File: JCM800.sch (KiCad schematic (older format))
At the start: 102 parts, among them U1 ECC83, U2 ECC83, U3 ECC83, U4 EL84, U5 EL84

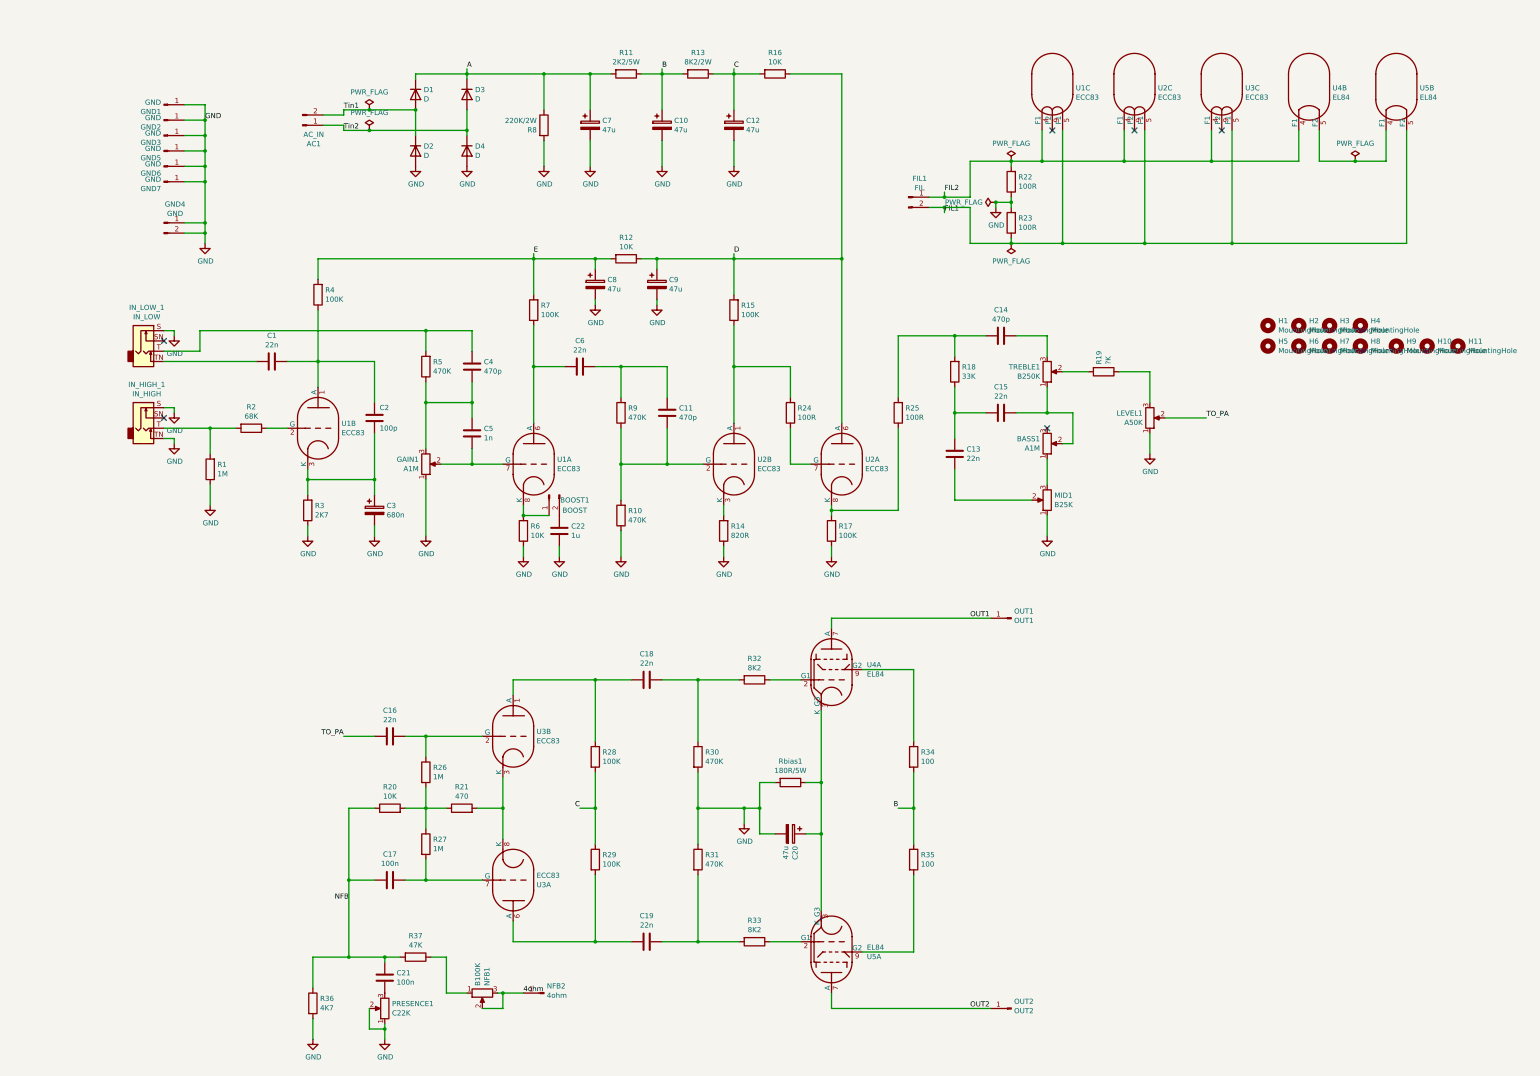
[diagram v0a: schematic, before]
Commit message: New grounding scheme
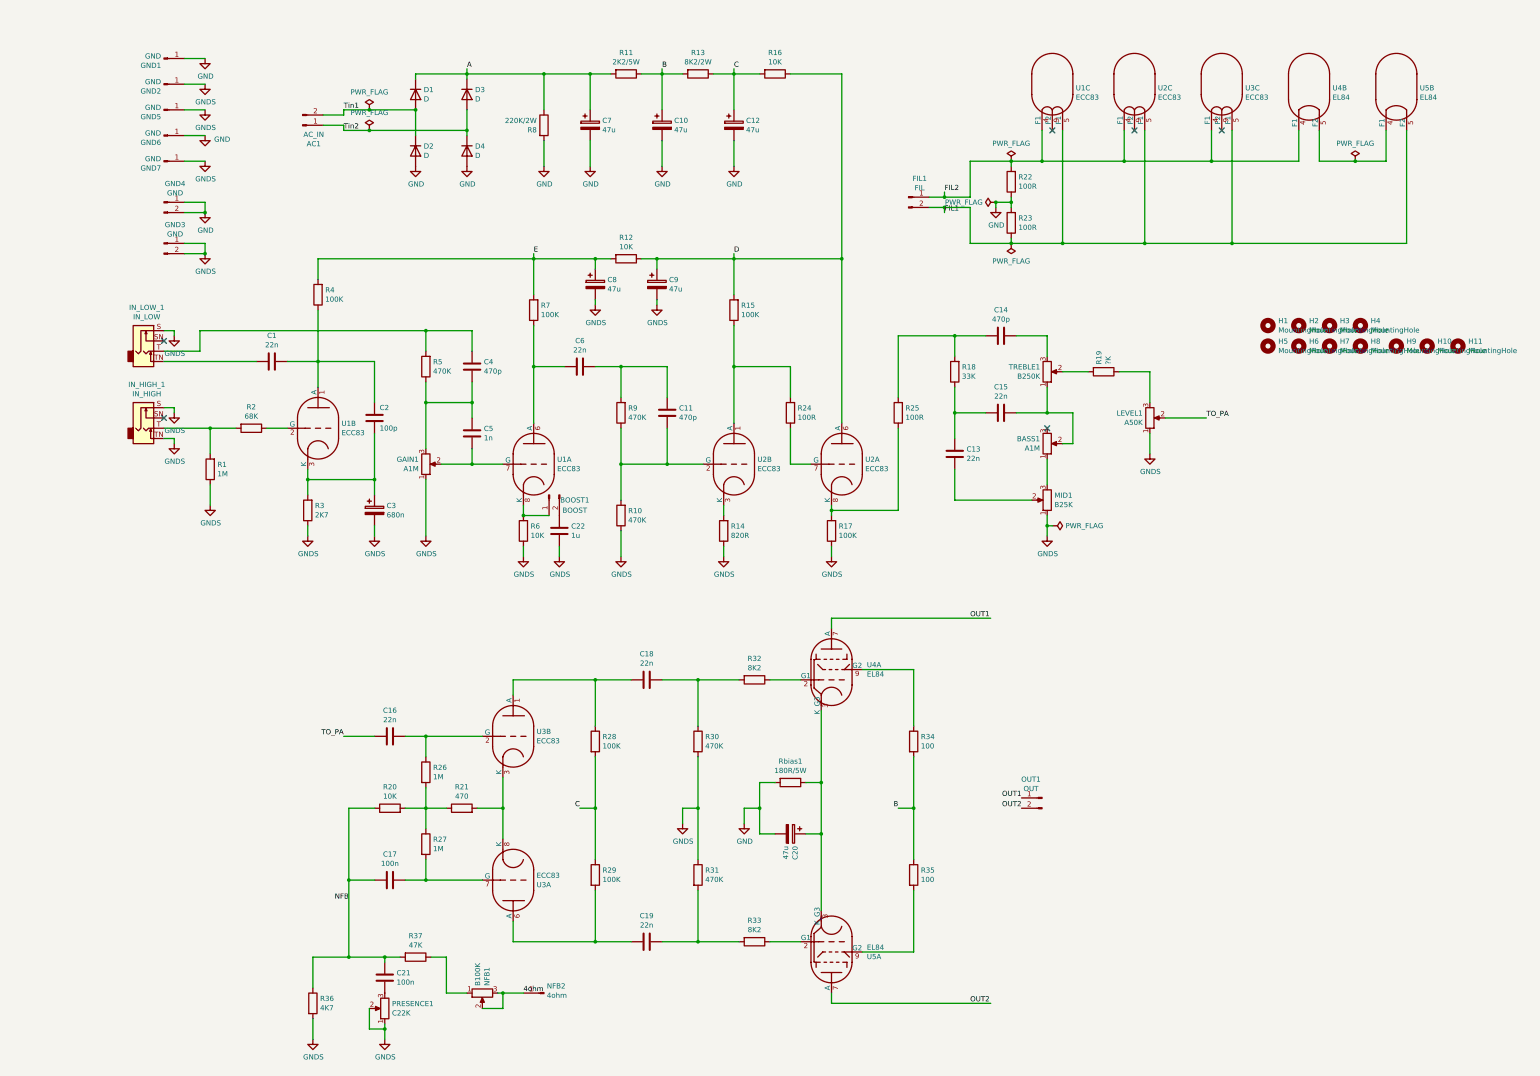
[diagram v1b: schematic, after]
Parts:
- removed GND3: GND, Connector_PinHeader_2.54mm:PinHeader_1x01_P2.54mm_Vertical, symbol Connector:Conn_01x01_Male
- removed OUT1: OUT1, Connector_PinHeader_2.54mm:PinHeader_1x01_P2.54mm_Vertical, symbol Connector:Conn_01x01_Male
- removed OUT2: OUT2, Connector_PinHeader_2.54mm:PinHeader_1x01_P2.54mm_Vertical, symbol Connector:Conn_01x01_Male
- added GND3: GND, TerminalBlock_MetzConnect:TerminalBlock_MetzConnect_Type094_RT03502HBLU_1x02_P5.00mm_Horizontal, symbol Connector:Conn_01x02_Male
- added GND6: GND, symbol power:GND
- added OUT1: OUT, TerminalBlock_MetzConnect:TerminalBlock_MetzConnect_Type094_RT03502HBLU_1x02_P5.00mm_Horizontal, symbol Connector:Conn_01x02_Male
- C20: footprint Capacitor_THT:CP_Radial_D7.5mm_P2.50mm -> Capacitor_THT:CP_Radial_D10.0mm_P3.50mm
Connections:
- net GND: now also GND6.1 (GND); no longer C22.2, C3.2, C8.2, C9.2, GAIN1.1, GND2.1 (Pin_1), GND5.1 (Pin_1), GND7.1 (Pin_1), IN_HIGH_1.S, IN_HIGH_1.TN, IN_LOW_1.S, LEVEL1.1, MID1.1, PRESENCE1.1, PRESENCE1.2, R1.1, R10.1, R14.1, R17.1, R3.1, R30.2, R31.1, R36.2, R6.1
- net OUT1: now also OUT1.1 (Pin_1)
- net OUT2: now also OUT1.2 (Pin_2)
- new net GNDS: C22.2, C3.2, C8.2, C9.2, GAIN1.1, GND2.1 (Pin_1), GND3.1 (Pin_1), GND3.2 (Pin_2), GND5.1 (Pin_1), GND7.1 (Pin_1), IN_HIGH_1.S, IN_HIGH_1.TN, IN_LOW_1.S, LEVEL1.1, MID1.1, PRESENCE1.1, PRESENCE1.2, R1.1, R10.1, R14.1, R17.1, R3.1, R30.2, R31.1, R36.2, R6.1
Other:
- moved on the sheet: GND1, GND2, GND4, GND5, GND6, GND7, R28, R29, R30, R31, R34, R35

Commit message: Screen resistor added
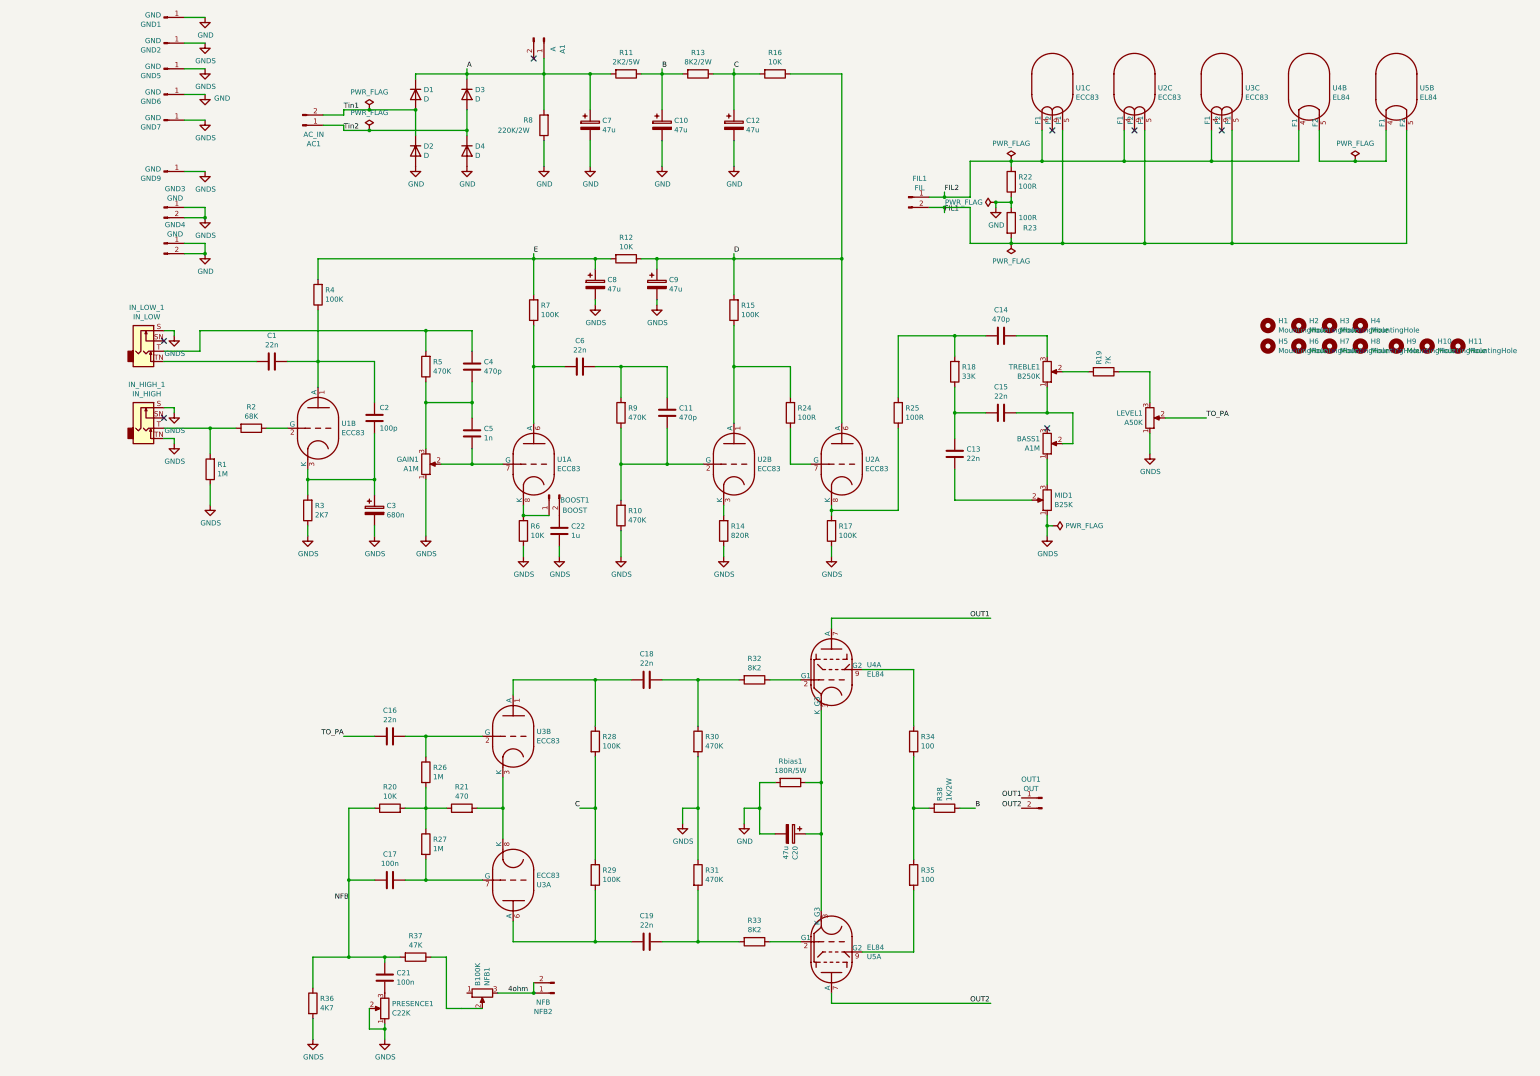
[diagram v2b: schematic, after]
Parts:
- removed GND6: GND, symbol power:GND
- removed NFB2: 4ohm, Connector_PinHeader_2.54mm:PinHeader_1x01_P2.54mm_Vertical, symbol Connector:Conn_01x01_Male
- added A1: A, TerminalBlock_MetzConnect:TerminalBlock_MetzConnect_Type094_RT03502HBLU_1x02_P5.00mm_Horizontal, symbol Connector:Conn_01x02_Male
- added GND9: GND, Connector_PinHeader_2.54mm:PinHeader_1x01_P2.54mm_Vertical, symbol Connector:Conn_01x01_Male
- added NFB2: NFB, TerminalBlock_MetzConnect:TerminalBlock_MetzConnect_Type094_RT03502HBLU_1x02_P5.00mm_Horizontal, symbol Connector:Conn_01x02_Male
- added R38: 1K/2W, Resistor_THT:R_Axial_DIN0414_L11.9mm_D4.5mm_P15.24mm_Horizontal, symbol Device:R
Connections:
- net 4ohm: now also NFB2.1 (Pin_1), NFB2.2 (Pin_2); no longer NFB1.2
- net A: now also R8.2, A1.1 (Pin_1); no longer R8.1
- net B: now also R38.1; no longer R34.2, R35.1
- net FIL1: now also R23.2; no longer R23.1
- net GND: now also R23.1, R8.1; no longer R23.2, R8.2
- net GNDS: now also GND9.1 (Pin_1)
- net at R37.1: now also NFB1.2; no longer NFB1.1
- new net: R34.2, R35.1, R38.2
- no-connect marks 6 -> 7
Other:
- moved on the sheet: GND1, GND2, GND3, GND4, GND5, GND6, GND7

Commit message: Preparing initial release
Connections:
- no-connect marks 7 -> 8
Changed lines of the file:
@@
 	5450 10200 5800 10200
 Wire Wire Line
-	5300 10350 5100 10350
+	4950 9850 4950 10350
+NoConn ~ 5150 10200
 Wire Wire Line
-	4950 10350 5100 10350
-Wire Wire Line
-	4950 9850 4950 10350
+	4950 10350 5300 10350
 $EndSCHEMATC

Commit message: Tweaks
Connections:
- net K: now reaches C20.1, Rbias1.1, U4.3 (K_G3), U5.3 (K_G3)
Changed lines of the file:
@@
 Wire Wire Line
 	4950 10350 5300 10350
+Text Label 8600 8400 0    50   ~ 0
+K
 $EndSCHEMATC

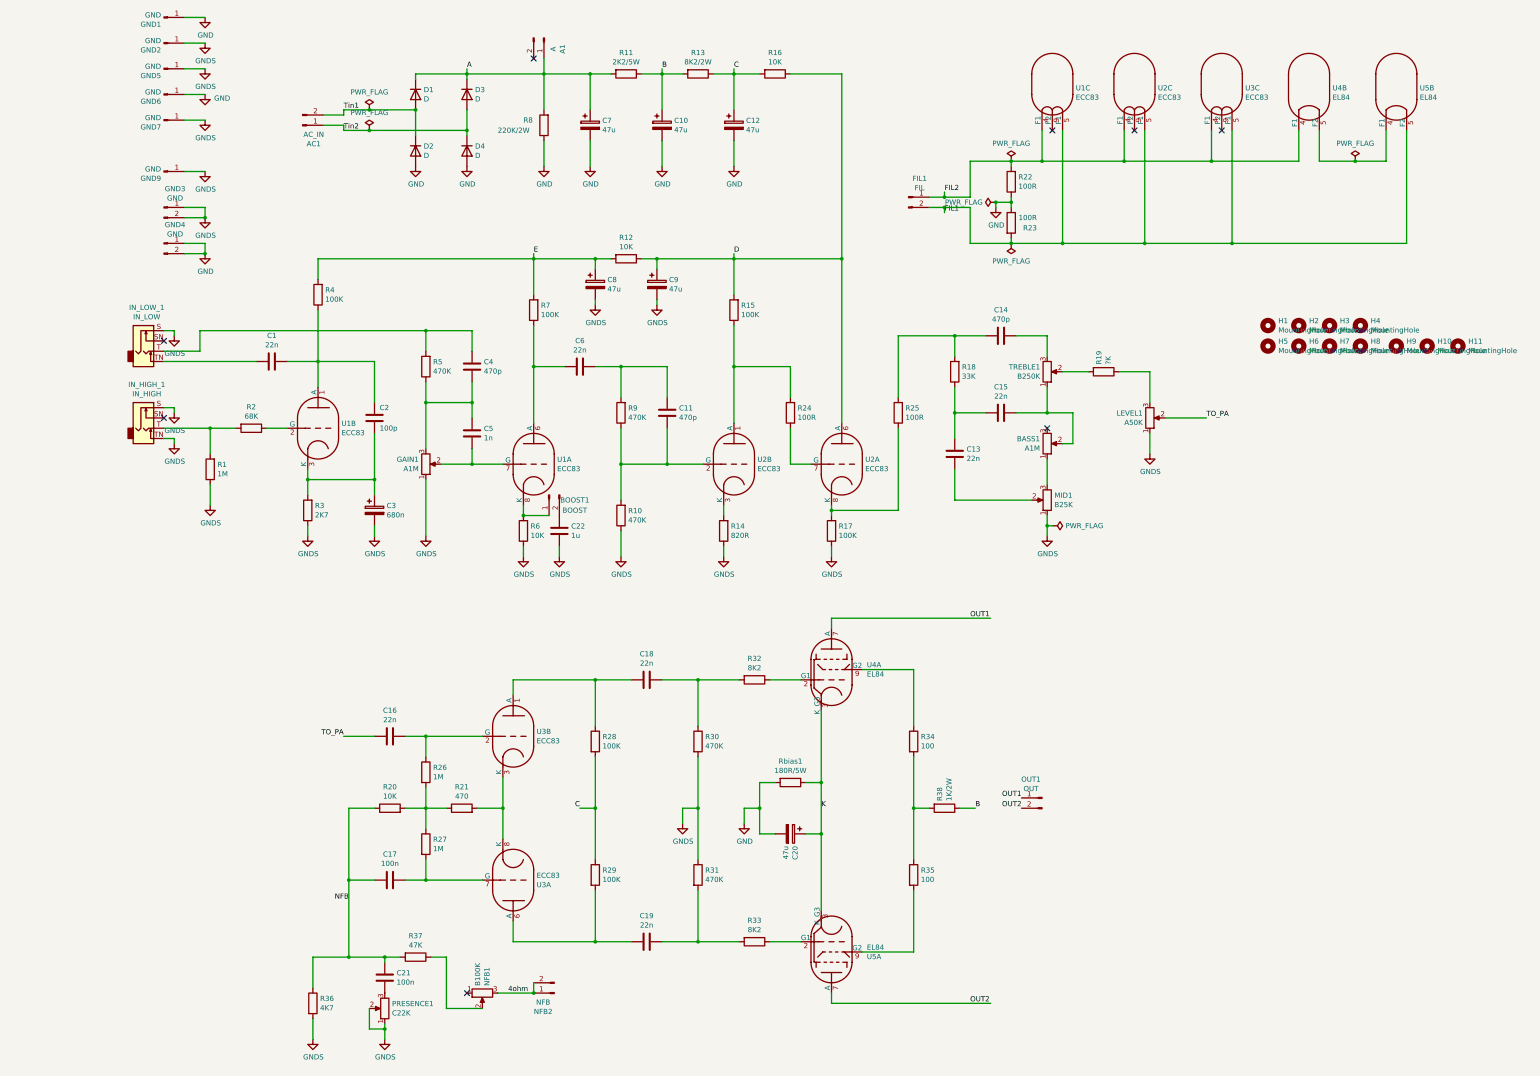
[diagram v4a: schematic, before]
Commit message: Fixed bias
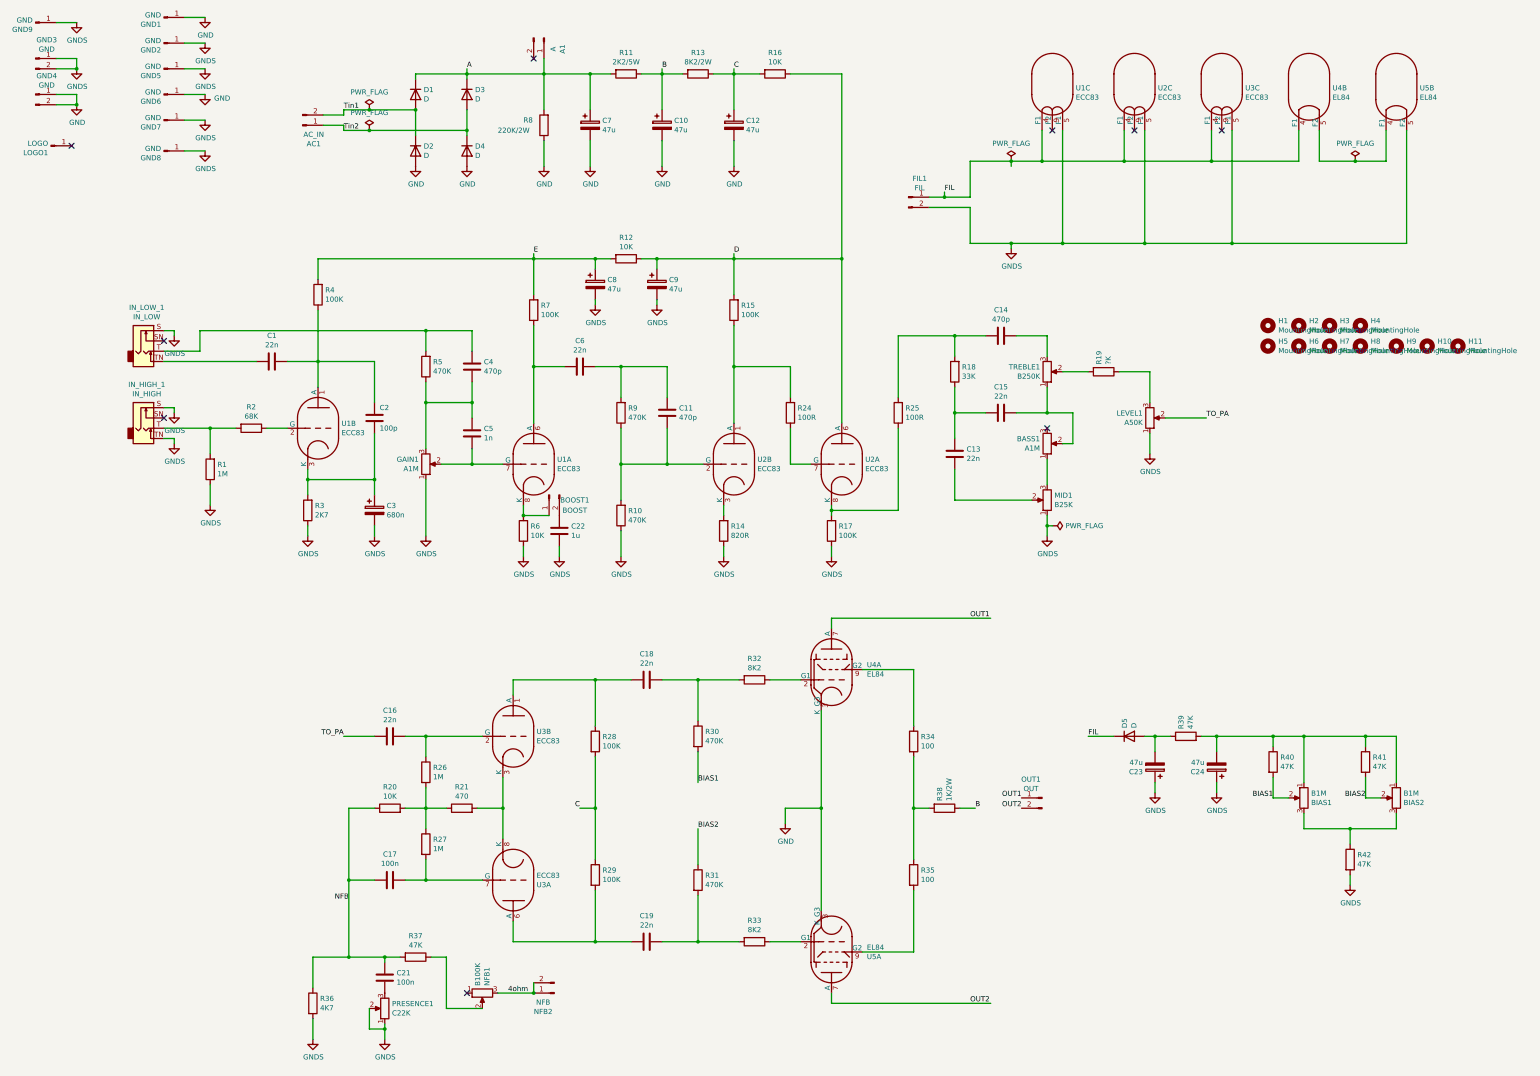
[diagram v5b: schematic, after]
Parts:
- removed C20: 47u, Capacitor_THT:CP_Radial_D10.0mm_P3.50mm, symbol Device:CP
- removed R22, R23: 100R, Resistor_THT:R_Axial_DIN0207_L6.3mm_D2.5mm_P10.16mm_Horizontal, symbol Device:R
- removed Rbias1: 180R/5W, Resistor_THT:R_Axial_DIN0922_L20.0mm_D9.0mm_P7.62mm_Vertical, symbol Device:R
- added BIAS1, BIAS2: B1M, Potentiometer_THT:Potentiometer_Bourns_3296W_Vertical, symbol Device:R_POT
- added C23, C24: 47u, Capacitor_THT:CP_Radial_D6.3mm_P2.50mm, symbol Device:CP
- added D5: D, Diode_THT:D_A-405_P10.16mm_Horizontal, symbol Device:D
- added GND8: GND, Connector_PinHeader_2.54mm:PinHeader_1x01_P2.54mm_Vertical, symbol Connector:Conn_01x01_Male
- added LOGO1: LOGO, toad-logo:toad-big, symbol Connector:Conn_01x01_Male
- added R39, R40, R41, R42: 47K, Resistor_THT:R_Axial_DIN0207_L6.3mm_D2.5mm_P10.16mm_Horizontal, symbol Device:R
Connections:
- net FIL1 is gone; now on net GNDS: FIL1.2 (Pin_2), U1.5 (F1), U2.5 (F1), U3.5 (F1), U5.5 (F2)
- net K is gone; now on net GND: U4.3 (K_G3), U5.3 (K_G3)
- net GNDS: now also C23.1, C24.1, GND8.1 (Pin_1), R42.2; no longer R30.2, R31.1
- net FIL2 renamed FIL
- net FIL: now also D5.1 (K)
- new net: C23.2, D5.2 (A), R39.1
- new net: BIAS1.1, BIAS2.1, C24.2, R39.2, R40.1, R41.1
- new net: BIAS1.3, BIAS2.3, R42.1
- new net BIAS1: BIAS1.2, R30.2, R40.2
- new net BIAS2: BIAS2.2, R31.1, R41.2
- no-connect marks 8 -> 9
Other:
- moved on the sheet: GND3, GND4, GND9, R30, R31

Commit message: Tweaks
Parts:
- C23, C24: value 47u -> 68u
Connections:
- net GND: now also GND5.1 (Pin_1)
- net GNDS: no longer GND5.1 (Pin_1)
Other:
- moved on the sheet: C21, NFB1, NFB2, PRESENCE1, R36, R37, R40, R41
